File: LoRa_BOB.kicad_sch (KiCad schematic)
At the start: 6 parts, among them U1 RFM95W-915S2

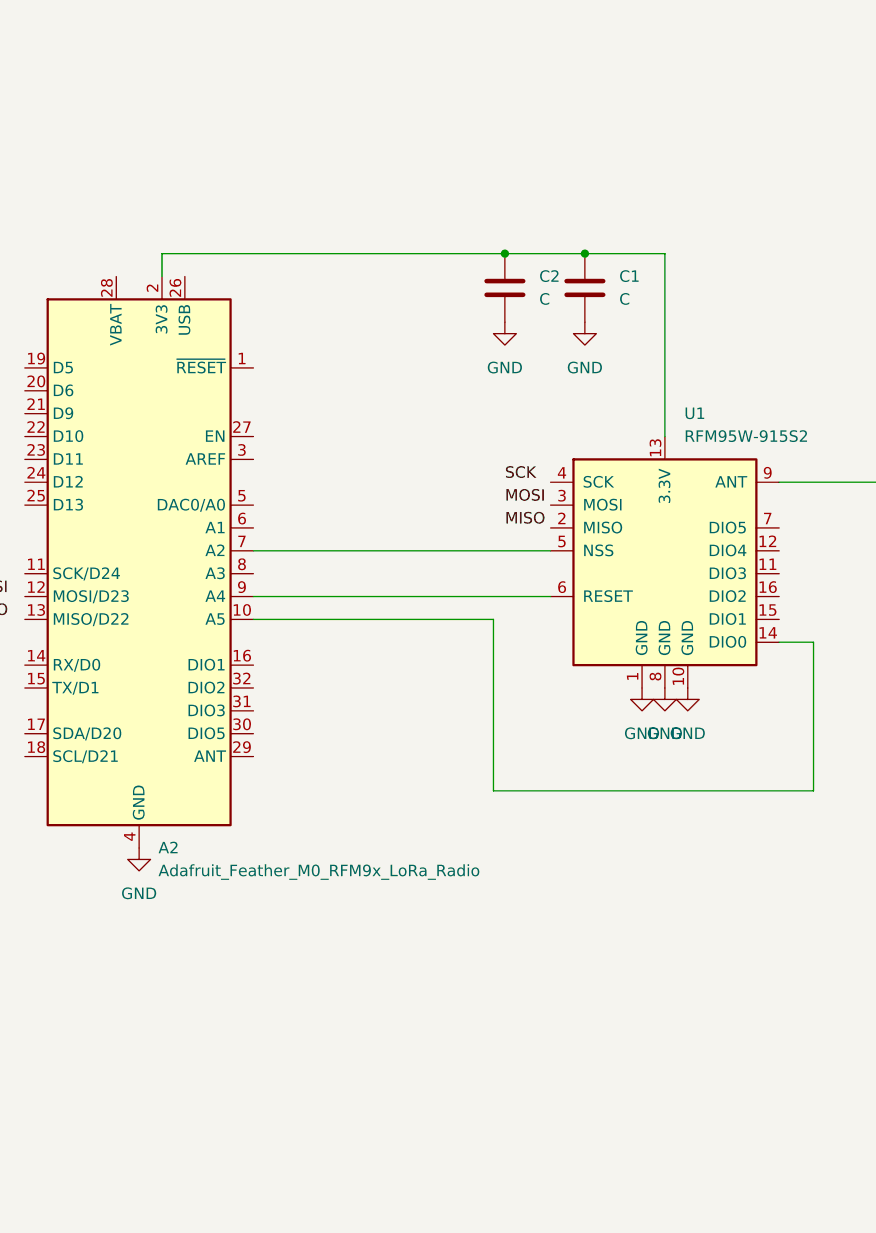
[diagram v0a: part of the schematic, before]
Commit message: Added regulator and placed level shifters
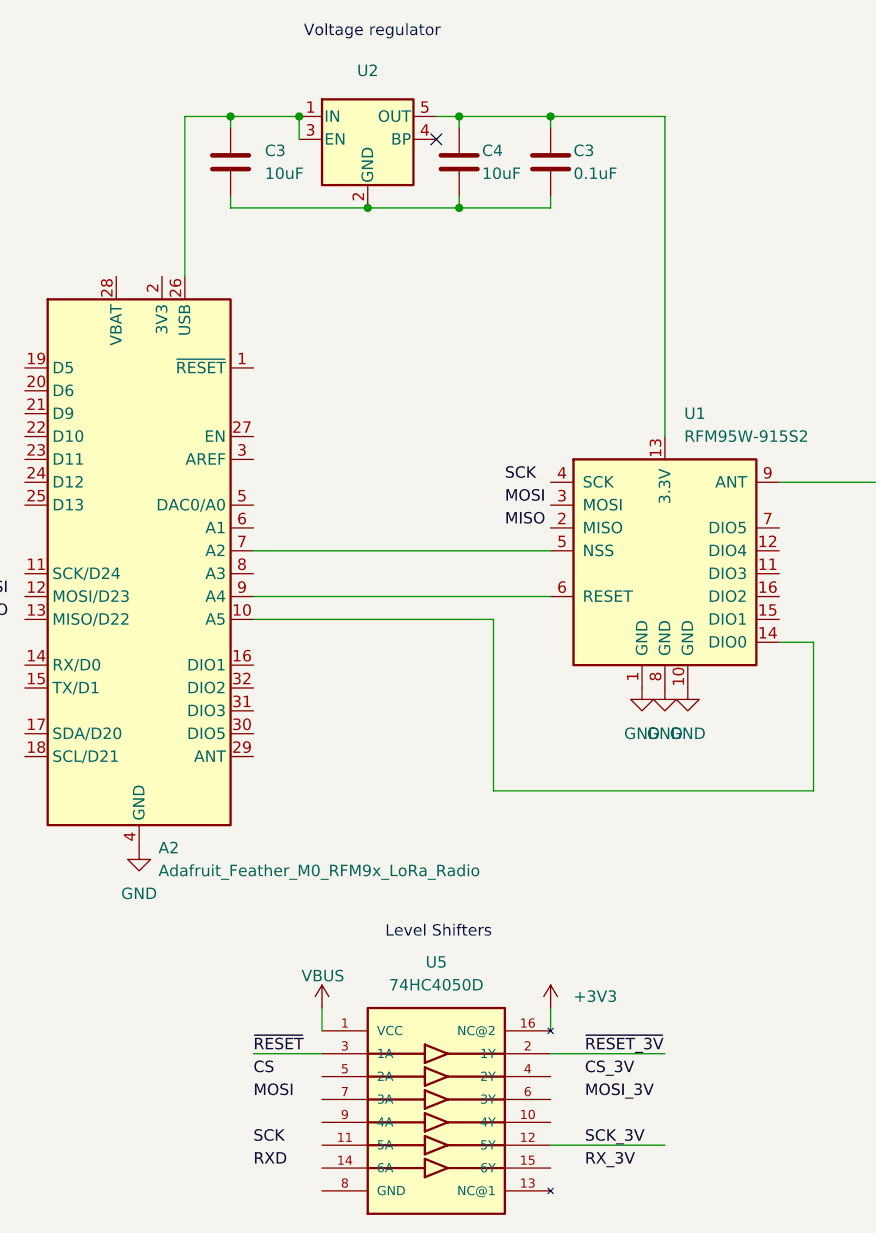
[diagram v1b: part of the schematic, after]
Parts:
- removed C1, C2: C, Capacitor_SMD:C_0805_2012Metric_Pad1.18x1.45mm_HandSolder, symbol Device:C
- added C3, C4: 10uF, Capacitor_SMD:C_1206_3216Metric_Pad1.33x1.80mm_HandSolder, symbol Device:C
- added C3: 0.1uF, Capacitor_SMD:C_0805_2012Metric_Pad1.18x1.45mm_HandSolder, symbol Device:C
- added U2: XC6210B332MR-G, Package_TO_SOT_SMD:SOT-23-5, symbol Regulator_Linear:MIC5205-3.3YM5
- added U5: 74HC4050D, Package_SO:SOIC-16_3.9x9.9mm_P1.27mm, symbol 74HC4050D:74HC4050D
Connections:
- net at U1.13 (3.3V): now also C3.1, C4.1, U2.5 (OUT); no longer A2.2 (3V3)
- net at A2.26 (USB): now also C3.1, U2.1 (IN), U2.3 (EN)
- new net: C3.2, C3.2, C4.2, U2.2 (GND)
- new net +3V3: U5.16 (NC@2)
- new net SCK_3V: U5.12 (5Y)
- new net VBUS: U5.1 (VCC)
- new net ~{RESET_3V}: U5.2 (1Y)
- new net ~{RESET}: U5.3 (1A)
- no-connect marks 0 -> 1
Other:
- note added: "Level Shifters"
- note added: "Voltage regulator"

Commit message: Minor advances
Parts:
- removed A1: Adafruit_Feather_Generic, Module:Adafruit_Feather, symbol MCU_Module:Adafruit_Feather_Generic
- renumbered A2 to A1, C3 to C1, C4 to C2, U2 to U1, U1 to U2, U5 to U3
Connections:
- net VBUS is gone; now on an unnamed net: U3.1 (VCC)
- net +3V3: now also C2.1, C3.1, U1.5 (OUT), U2.13 (3.3V)
- net CS: now also A1.7 (A2), U3.5 (2A)
- net CS_3V: now also U2.5 (NSS), U3.4 (2Y)
- net MISO: now also A1.13 (MISO/D22), U2.2 (MISO)
- net MOSI: now also A1.12 (MOSI/D23), U3.7 (3A)
- net MOSI_3V: now also U2.3 (MOSI), U3.6 (3Y)
- net SCK: now also A1.11 (SCK/D24), U3.11 (5A)
- net SCK_3V: now also U2.4 (SCK)
- net ~{RESET}: now also A1.6 (A1)
- net at A1.16 (DIO1): now also U2.15 (DIO1)
- net at A1.9 (A4): now also U3.9 (4A); no longer U2.6 (RESET)
- net at U3.10 (4Y): now also U2.6 (RESET)
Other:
- note added: "LDO Voltage regulator"
- note added: "Level Shifters Layout Practice and in case the Featherwing is connected to an Arduino"
- note added: "LoRa Transceiver"
- note removed: "Level Shifters"
- note removed: "Voltage regulator"
- moved on the sheet: A1, AE1, C1, C2, C3, U1, U2, U3

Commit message: Routed but could be better
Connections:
- net +3V3: now also U3.1 (VCC); no longer U3.16 (NC@2)
- net GND: now also C1.2, C2.2, C3.2, U1.2 (GND), U3.8 (GND)
- net at A1.2 (3V3): no longer U3.1 (VCC)
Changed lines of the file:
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@@
-	(wire
-		(pts
-			(xy 158.75 105.41) (xy 176.53 105.41)
-		)
-		(stroke
-			(width 0)
-			(type default)
-		)
-	)
 	(wire
 		(pts
@@
 	(wire
 		(pts
-			(xy 220.98 130.81) (xy 220.98 133.35)
-		)
-		(stroke
-			(width 0)
-			(type default)
-		)
-	)
-	(wire
-		(pts
 			(xy 220.98 135.89) (xy 233.68 135.89)
 		)
@@
 	(wire
 		(pts
-			(xy 176.53 105.41) (xy 176.53 133.35)
-		)
-		(stroke
-			(width 0)
-			(type default)
-		)
-	)
-	(wire
-		(pts
 			(xy 264.16 92.71) (xy 264.16 125.73)
 		)
@@
 	(wire
 		(pts
-			(xy 176.53 133.35) (xy 195.58 133.35)
-		)
-		(stroke
-			(width 0)
-			(type default)
-		)
-	)
-	(wire
-		(pts
 			(xy 184.15 160.02) (xy 284.48 160.02)
 		)
@@
 		(pts
 			(xy 289.56 128.27) (xy 289.56 130.81)
-		)
-		(stroke
-			(width 0)
-			(type default)
-		)
-	)
-	(wire
-		(pts
-			(xy 158.75 107.95) (xy 158.75 105.41)
 		)
 		(stroke
@@
 	(symbol
 		(lib_id "power:+3V3")
-		(at 220.98 130.81 0)
+		(at 195.58 133.35 0)
 		(unit 1)
 		(exclude_from_sim no)
@@
 		(on_board yes)
 		(dnp no)
-		(fields_autoplaced yes)
 		(property "Reference" "#PWR02"
-			(at 220.98 134.62 0)
+			(at 195.58 137.16 0)
 			(effects
 				(font
@@
 		)
 		(property "Value" "+3V3"
-			(at 223.52 129.5399 0)
+			(at 192.532 129.54 0)
 			(effects
 				(font
@@
 		)
 		(property "Footprint" ""
-			(at 220.98 130.81 0)
+			(at 195.58 133.35 0)
 			(effects
 				(font
@@
 		)
 		(property "Datasheet" ""
-			(at 220.98 130.81 0)
+			(at 195.58 133.35 0)
 			(effects
 				(font
@@
 		)
 		(property "Description" "Power symbol creates a global label with name \"+3V3\""
-			(at 220.98 130.81 0)
+			(at 195.58 133.35 0)
 			(effects
 				(font
@@
 	)
 	(symbol
+		(lib_id "power:GND")
+		(at 195.58 151.13 0)
+		(unit 1)
+		(exclude_from_sim no)
+		(in_bom yes)
+		(on_board yes)
+		(dnp no)
+		(fields_autoplaced yes)
+		(property "Reference" "#PWR07"
+			(at 195.58 157.48 0)
+			(effects
+				(font
+					(size 1.27 1.27)
+				)
+				(hide yes)
+			)
+		)
+		(property "Value" "GND"
+			(at 195.58 156.21 0)
+			(effects
+				(font
+					(size 1.27 1.27)
+				)
+			)
+		)
+		(property "Footprint" ""
+			(at 195.58 151.13 0)
+			(effects
+				(font
+					(size 1.27 1.27)
+				)
+				(hide yes)
+			)
+		)
+		(property "Datasheet" ""
+			(at 195.58 151.13 0)
+			(effects
+				(font
+					(size 1.27 1.27)
+				)
+				(hide yes)
+			)
+		)
+		(property "Description" "Power symbol creates a global label with name \"GND\" , ground"
+			(at 195.58 151.13 0)
+			(effects
+				(font
+					(size 1.27 1.27)
+				)
+				(hide yes)
+			)
+		)
+		(pin "1"
+		)
+		(instances
+			(project "LoRa_BOB"
+				(path "/bd24c4db-4e36-4117-bd4f-5228ef241da9"
+					(reference "#PWR07")
+					(unit 1)
+				)
+			)
+		)
+	)
+	(symbol
 		(lib_id "MCU_Module:Adafruit_Feather_M0_RFM9x_LoRa_Radio")
 		(at 156.21 138.43 0)
@@
 					(unit 1)
 				)
+			)
+		)
+	)
+	(symbol
+		(lib_id "power:GND")
+		(at 203.2 102.87 0)
+		(unit 1)
+		(exclude_from_sim no)
+		(in_bom yes)
+		(on_board yes)
+		(dnp no)
+		(fields_autoplaced yes)
+		(property "Reference" "#PWR08"
+			(at 203.2 109.22 0)
+			(effects
+				(font
+					(size 1.27 1.27)
+				)
+				(hide yes)
+			)
+		)
+		(property "Value" "GND"
+			(at 203.2 107.95 0)
+			(effects
+				(font
+					(size 1.27 1.27)
+				)
+			)
+		)
+		(property "Footprint" ""
+			(at 203.2 102.87 0)
+			(effects
+				(font
+					(size 1.27 1.27)
+				)
+				(hide yes)
+			)
+		)
+		(property "Datasheet" ""
+			(at 203.2 102.87 0)
+			(effects
+				(font
+					(size 1.27 1.27)
+				)
+				(hide yes)
+			)
+		)
+		(property "Description" "Power symbol creates a global label with name \"GND\" , ground"
+			(at 203.2 102.87 0)
+			(effects
+				(font
+					(size 1.27 1.27)
+				)
+				(hide yes)
+			)
+		)
+		(pin "1"
+		)
+		(instances
+			(project "LoRa_BOB"
+				(path "/bd24c4db-4e36-4117-bd4f-5228ef241da9"
+					(reference "#PWR08")
+					(unit 1)
+				)

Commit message: New Template
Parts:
- removed AE1: Antenna, RF_Antenna:Texas_SWRA416_868MHz_915MHz, symbol Device:Antenna
- removed U1: XC6210B332MR-G, Package_TO_SOT_SMD:SOT-23-5, symbol Regulator_Linear:MIC5205-3.3YM5
- removed U2: RFM95W-915S2, RF_Module:HOPERF_RFM9XW_SMD, symbol RF_Module:RFM95W-915S2
- added U1: RFM97W-915S2, symbol RF_Module:RFM97W-915S2
- added U2: XC6210B332MR-G, Package_TO_SOT_SMD:SOT-23-5, symbol Regulator_Linear:MIC5205-3.3YM5
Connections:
- net +3V3: now also U2.5 (OUT)
- net CS_3V: now also U1.5 (NSS)
- net GND: now also U2.2 (GND); no longer A1.4 (GND)
- net MOSI: no longer A1.12 (MOSI/D23)
- net SCK: no longer A1.11 (SCK/D24)
- net SCK_3V: now also U1.4 (SCK)
- net at C1.1: now also U2.1 (IN), U2.3 (EN); no longer A1.26 (USB)
- net at U3.10 (4Y): now also U1.6 (RESET)
- net MISO: no longer names the net of A1.13 (MISO/D22)
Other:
- note removed: "LoRa Transceiver"
- company: designer: <me>@stanford.edu -> designer: pmahowld@stanford.edu
- title: Test sheet -> LoRa_BOB
- moved on the sheet: C1, C2, C3, U3

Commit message: basic, with trick Feather and RFM
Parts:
- U1: footprint (none) -> RF_Module:HOPERF_RFM9XW_SMD
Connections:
- net +3V3: now also U1.13 (3.3V)
- net GND: now also U1.1 (GND), U1.10 (GND), U1.8 (GND)
- net MOSI_3V: now also U1.3 (MOSI)
- net at C1.1, U2.1 (IN), U2.3 (EN): now also A1.26 (USB)
- net at A1.10 (A5): now also U1.14 (DIO0)
- net at A1.16 (DIO1): now also U1.15 (DIO1)
- net at A1.9 (A4): no longer U3.9 (4A)
- net at U1.6 (RESET): no longer U3.10 (4Y)
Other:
- moved on the sheet: C1, C2, C3, U2

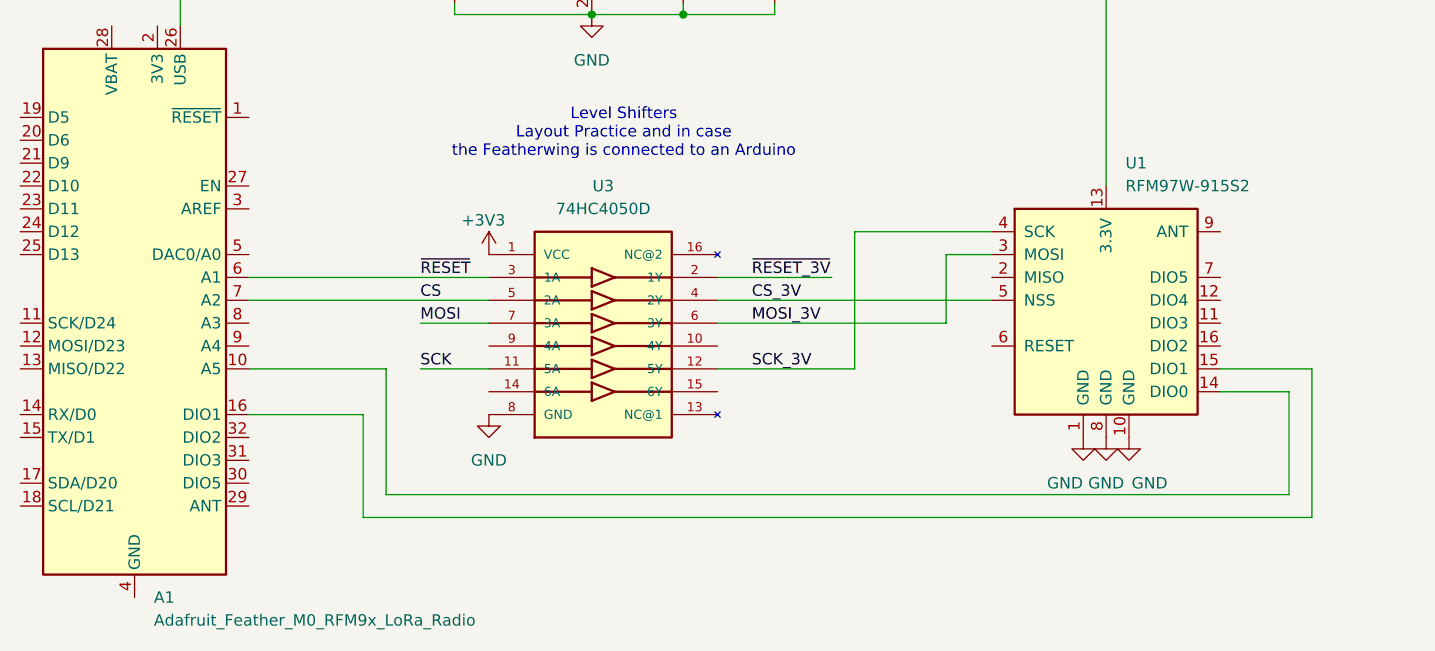
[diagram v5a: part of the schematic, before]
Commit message: edited existing footprints and symbol
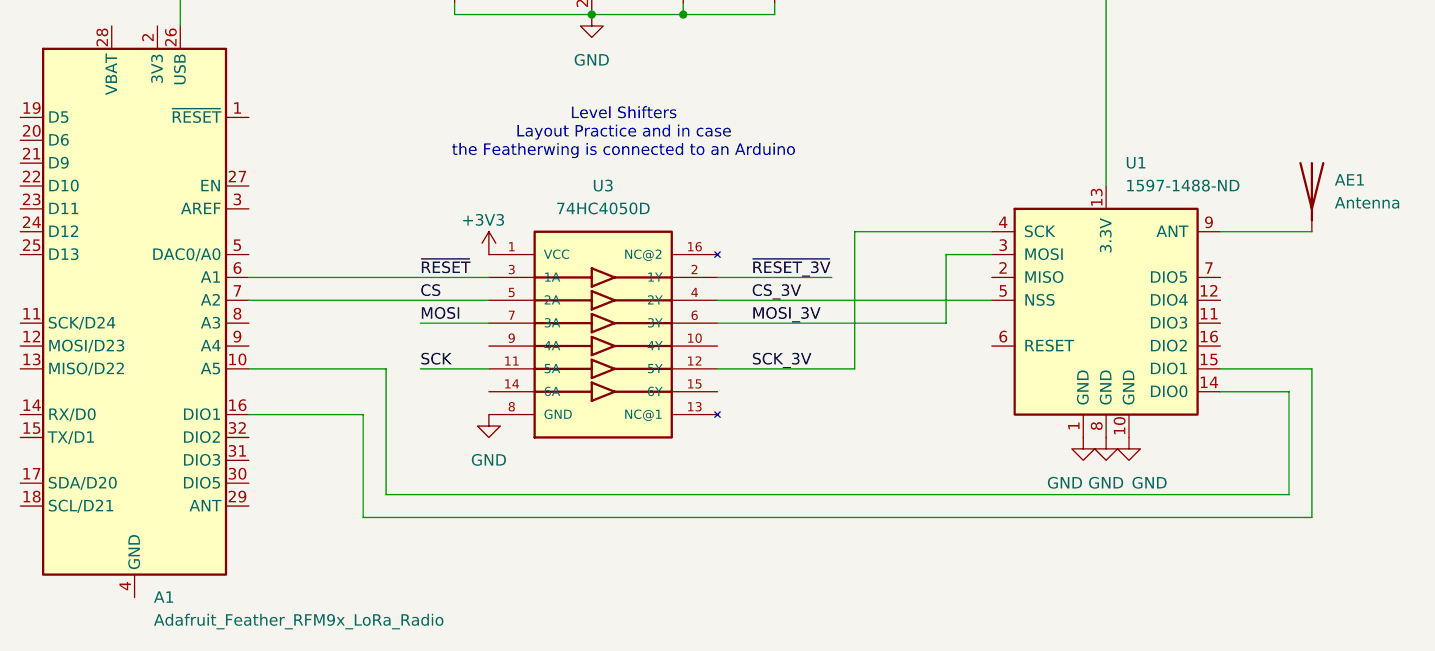
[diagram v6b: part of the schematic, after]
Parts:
- added AE1: Antenna, RF_Antenna:Texas_SWRA416_868MHz_915MHz, symbol Device:Antenna
- A1: value Adafruit_Feather_M0_RFM9x_LoRa_Radio -> Adafruit_Feather_RFM9x_LoRa_Radio
- U1: value RFM97W-915S2 -> 1597-1488-ND
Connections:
- net at U1.9 (ANT): now also AE1.1 (A)
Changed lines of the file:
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@@
+	(wire
+		(pts
+			(xy 292.1 114.3) (xy 302.26 114.3)
+		)
+		(stroke
+			(width 0)
+			(type default)
+		)
+	)
 	(wire
 		(pts
@@
 			)
 		)
-		(property "Value" "Adafruit_Feather_M0_RFM9x_LoRa_Radio"
+		(property "Value" "Adafruit_Feather_RFM9x_LoRa_Radio"
 			(at 173.5933 157.48 0)
 			(effects
@@
 			)
 		)
-		(property "Datasheet" "https://cdn-learn.adafruit.com/downloads/pdf/adafruit-feather-m0-radio-with-lora-radio-module.pdf"
+		(property "Datasheet" ""
 			(at 171.45 142.24 0)
 			(effects
@@
 			)
 		)
-		(property "Description" "Microcontroller module with SAMD21 Cortex-M0 MCU and RFM9x Radio"
+		(property "Description" "Featherwing RFM9x Radio"
 			(at 171.45 121.92 0)
 			(effects
@@
 			)
 		)
-		(property "Value" "RFM97W-915S2"
+		(property "Value" "1597-1488-ND"
 			(at 281.5433 109.22 0)
 			(effects
@@
 			)
 		)
-		(property "Datasheet" "https://www.hoperf.com/data/upload/portal/20181127/5bfcbea20e9ef.pdf"
+		(property "Datasheet" "https://github.com/SeeedDocument/RFM95-98_LoRa_Module/blob/master/RFM95_96_97_98_DataSheet.pdf"
 			(at 195.58 80.01 0)
 			(effects
@@
 					(unit 1)
 				)
+			)
+		)
+	)
+	(symbol
+		(lib_id "Device:Antenna")
+		(at 302.26 109.22 0)
+		(unit 1)
+		(exclude_from_sim no)
+		(in_bom yes)
+		(on_board yes)
+		(dnp no)
+		(fields_autoplaced yes)
+		(property "Reference" "AE1"
+			(at 304.8 108.5849 0)
+			(effects
+				(font
+					(size 1.27 1.27)
+				)
+				(justify left)
+			)
+		)
+		(property "Value" "Antenna"
+			(at 304.8 111.1249 0)
+			(effects
+				(font
+					(size 1.27 1.27)
+				)
+				(justify left)
+			)
+		)
+		(property "Footprint" "RF_Antenna:Texas_SWRA416_868MHz_915MHz"
+			(at 302.26 109.22 0)
+			(effects
+				(font
+					(size 1.27 1.27)
+				)
+				(hide yes)
+			)
+		)
+		(property "Datasheet" "~"
+			(at 302.26 109.22 0)
+			(effects
+				(font
+					(size 1.27 1.27)
+				)
+				(hide yes)
+			)
+		)
+		(property "Description" "Antenna"
+			(at 302.26 109.22 0)
+			(effects
+				(font
+					(size 1.27 1.27)
+				)
+				(hide yes)
+			)
+		)
+		(pin "1"
+		)
+		(instances
+			(project ""
+				(path "/bd24c4db-4e36-4117-bd4f-5228ef241da9"
+					(reference "AE1")
+					(unit 1)
+				)

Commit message: pours
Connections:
- net GND: now also A1.4 (GND)
- net MOSI: now also A1.12 (MOSI/D23)
- net SCK: now also A1.11 (SCK/D24)
- net ~{RESET_3V}: now also U1.6 (RESET)
- net MISO: now reaches A1.13 (MISO/D22)
- net MISO: now also U1.2 (MISO)
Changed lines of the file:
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@@
+	(wire
+		(pts
+			(xy 257.81 127) (xy 266.7 127)
+		)
+		(stroke
+			(width 0)
+			(type default)
+		)
+	)
 	(wire
 		(pts
@@
 	(wire
 		(pts
+			(xy 153.67 124.46) (xy 158.75 124.46)
+		)
+		(stroke
+			(width 0)
+			(type default)
+		)
+	)
+	(wire
+		(pts
 			(xy 292.1 114.3) (xy 302.26 114.3)
 		)
@@
 	(wire
 		(pts
-			(xy 261.62 116.84) (xy 266.7 116.84)
+			(xy 256.54 116.84) (xy 266.7 116.84)
 		)
 		(stroke
@@
 	(wire
 		(pts
-			(xy 236.22 124.46) (xy 261.62 124.46)
+			(xy 236.22 124.46) (xy 256.54 124.46)
 		)
 		(stroke
@@
 	(wire
 		(pts
+			(xy 153.67 129.54) (xy 158.75 129.54)
+		)
+		(stroke
+			(width 0)
+			(type default)
+		)
+	)
+	(wire
+		(pts
 			(xy 203.2 129.54) (xy 210.82 129.54)
 		)
@@
 	(wire
 		(pts
+			(xy 153.67 127) (xy 158.75 127)
+		)
+		(stroke
+			(width 0)
+			(type default)
+		)
+	)
+	(wire
+		(pts
 			(xy 184.15 121.92) (xy 210.82 121.92)
 		)
@@
 	(wire
 		(pts
-			(xy 261.62 124.46) (xy 261.62 116.84)
+			(xy 256.54 124.46) (xy 256.54 116.84)
 		)
 		(stroke
@@
 		(pts
 			(xy 236.22 121.92) (xy 266.7 121.92)
+		)
+		(stroke
+			(width 0)
+			(type default)
+		)
+	)
+	(wire
+		(pts
+			(xy 261.62 119.38) (xy 266.7 119.38)
 		)
 		(stroke
@@
 		)
 	)
+	(label "MISO"
+		(at 261.62 119.38 0)
+		(effects
+			(font
+				(size 1.27 1.27)
+			)
+			(justify left bottom)
+		)
+	)
 	(label "MOSI_3V"
 		(at 240.03 124.46 0)
@@
 		)
 	)
+	(label "SCK"
+		(at 153.67 124.46 0)
+		(effects
+			(font
+				(size 1.27 1.27)
+			)
+			(justify left bottom)
+		)
+	)
+	(label "MISO"
+		(at 153.67 129.54 0)
+		(effects
+			(font
+				(size 1.27 1.27)
+			)
+			(justify left bottom)
+		)
+	)
 	(label "MOSI"
 		(at 203.2 124.46 0)
@@
 		)
 	)
+	(label "~{RESET_3V}"
+		(at 257.81 127 0)
+		(effects
+			(font
+				(size 1.27 1.27)
+			)
+			(justify left bottom)
+		)
+	)
 	(label "CS_3V"
 		(at 240.03 121.92 0)
@@
 	(label "SCK"
 		(at 203.2 129.54 0)
+		(effects
+			(font
+				(size 1.27 1.27)
+			)
+			(justify left bottom)
+		)
+	)
+	(label "MOSI"
+		(at 153.67 127 0)
 		(effects
 			(font
@@
 		(pin "10"
 		)
-		(pin "29"
-		)
 		(pin "32"
 		)
@@
 					(unit 1)
 				)
+			)
+		)
+	)
+	(symbol
+		(lib_id "power:GND")
+		(at 171.45 154.94 0)
+		(unit 1)
+		(exclude_from_sim no)
+		(in_bom yes)
+		(on_board yes)
+		(dnp no)
+		(fields_autoplaced yes)
+		(property "Reference" "#PWR06"
+			(at 171.45 161.29 0)
+			(effects
+				(font
+					(size 1.27 1.27)
+				)
+				(hide yes)
+			)
+		)
+		(property "Value" "GND"
+			(at 171.45 160.02 0)
+			(effects
+				(font
+					(size 1.27 1.27)
+				)
+			)
+		)
+		(property "Footprint" ""
+			(at 171.45 154.94 0)
+			(effects
+				(font
+					(size 1.27 1.27)
+				)
+				(hide yes)
+			)
+		)
+		(property "Datasheet" ""
+			(at 171.45 154.94 0)
+			(effects
+				(font
+					(size 1.27 1.27)
+				)
+				(hide yes)
+			)
+		)
+		(property "Description" "Power symbol creates a global label with name \"GND\" , ground"
+			(at 171.45 154.94 0)
+			(effects
+				(font
+					(size 1.27 1.27)
+				)
+				(hide yes)
+			)
+		)
+		(pin "1"
+		)
+		(instances
+			(project "LoRa_BOB"
+				(path "/bd24c4db-4e36-4117-bd4f-5228ef241da9"
+					(reference "#PWR06")
+					(unit 1)
+				)
